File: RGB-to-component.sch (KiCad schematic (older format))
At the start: 56 parts, among them J1 VGA, J3 USB_C_Receptacle_Power, J4 SCART_CONN, J5 3xRCA_CONN, U1 SC6206B-65K5, U2 TPF144-VR, U3 RS8752XQ, U4 TPF-141TR, U6 74AHC1G86, U7 74AHC1G86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

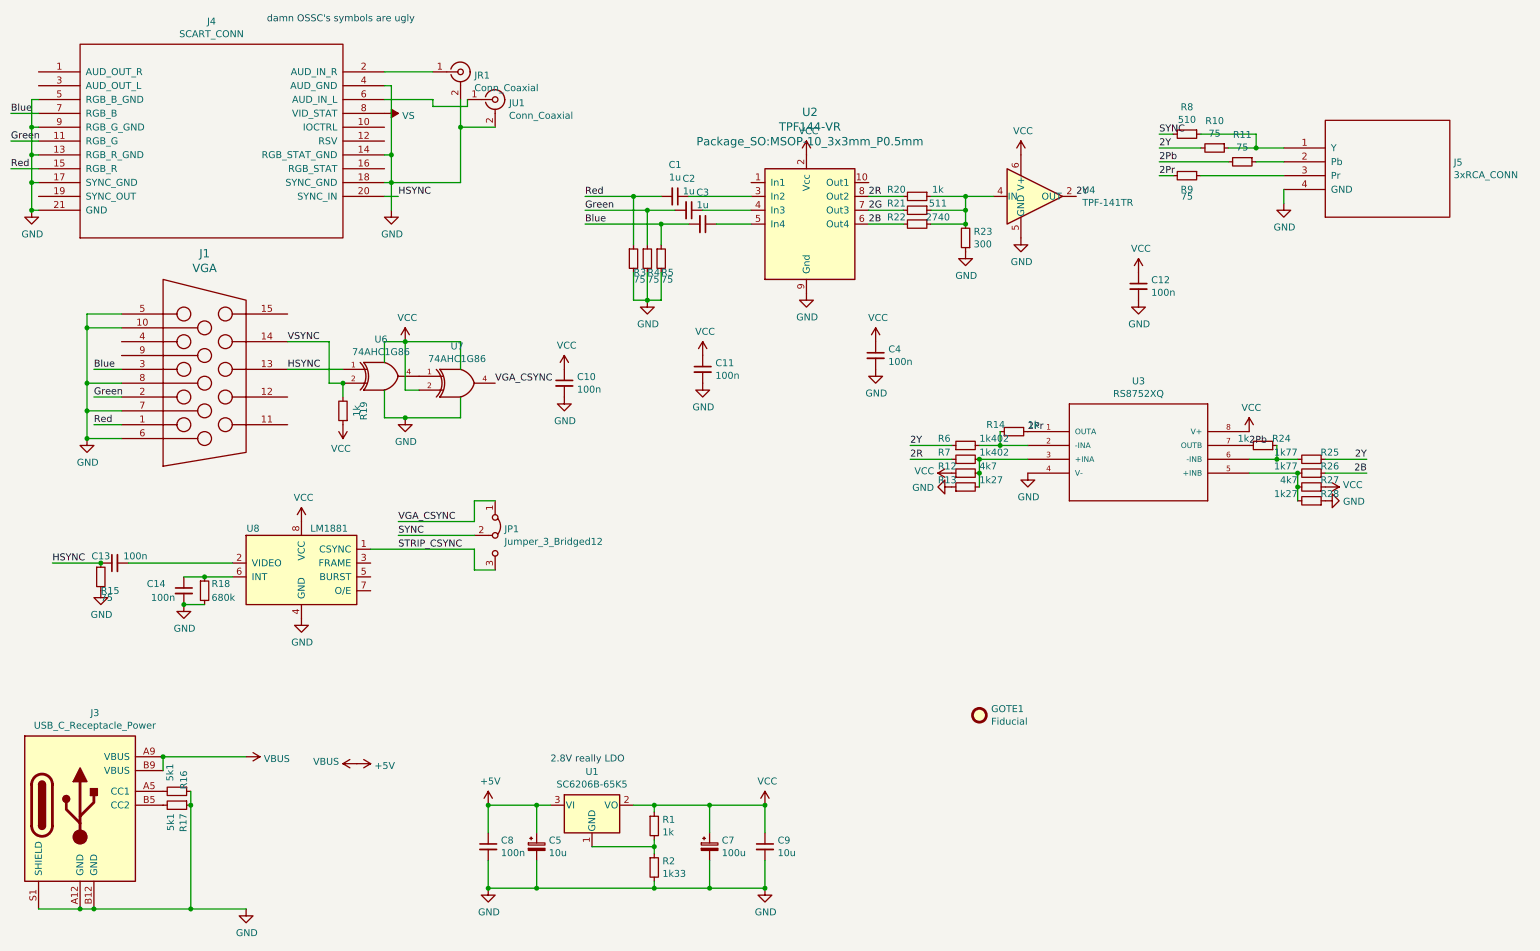
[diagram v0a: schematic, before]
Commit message: reusing video amp, ferrite, power led, updated jlc files
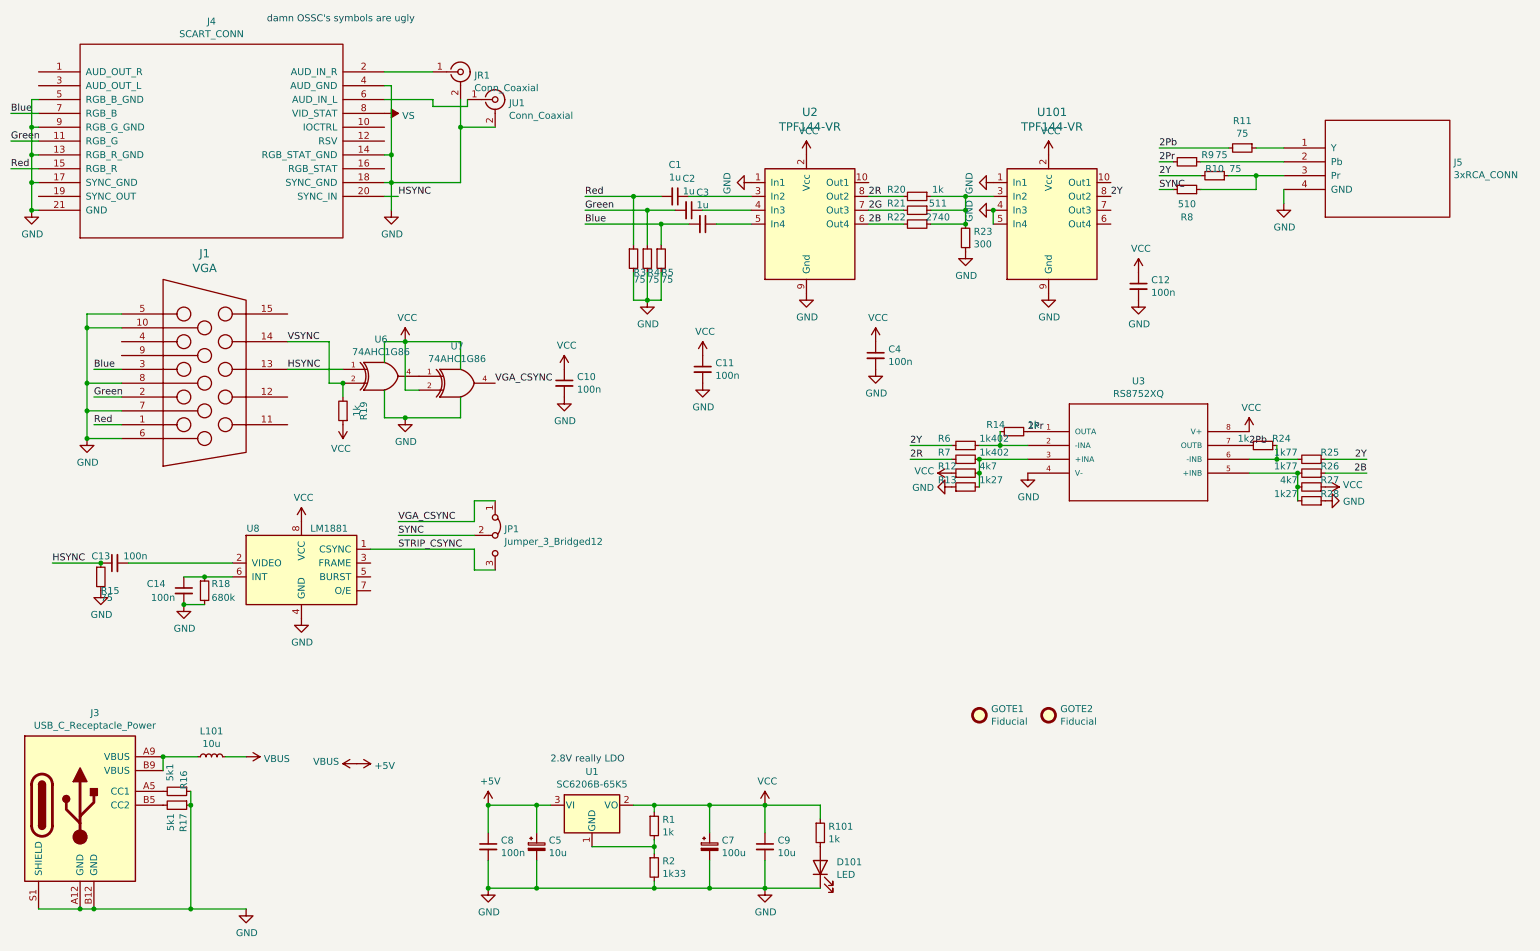
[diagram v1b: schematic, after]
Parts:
- removed U4: TPF-141TR, Package_TO_SOT_SMD:SOT-23-6, symbol Videobits:TPF-141TR
- added D101: LED, LED_SMD:LED_0805_2012Metric, symbol Device:LED
- added GOTE2: Fiducial, videobits:borgar, symbol Mechanical:Fiducial
- added L101: 10u, Inductor_SMD:L_0805_2012Metric_Pad1.15x1.40mm_HandSolder, symbol Device:L_Small
- added R101: 1k, Resistor_SMD:R_0805_2012Metric_Pad1.15x1.40mm_HandSolder, symbol Device:R_Small
- added U101: TPF144-VR, Package_SO:MSOP-10_3x3mm_P0.5mm, symbol Videobits:TPF144-VR
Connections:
- net +5V: now also L101.2; no longer J3.A9 (VBUS), J3.B9 (VBUS)
- net 2Y: now also U101.8 (Out2)
- net GND: now also U2.1 (In1), D101.1 (K), U101.1 (In1), U101.4 (In3), U101.5 (In4), U101.9 (Gnd)
- net VCC: now also R101.1, U101.2 (Vcc)
- net at R11.1: now also J5.1 (Y); no longer J5.2 (Pb)
- net at R10.1, R8.1: now also J5.3 (Pr); no longer J5.1 (Y)
- net at R9.1: now also J5.2 (Pb); no longer J5.3 (Pr)
- net at R20.1, R21.1, R22.1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: now also U101.3 (In2)
- new net: J3.A9 (VBUS), J3.B9 (VBUS), L101.1
- new net: D101.2 (A), R101.2
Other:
- moved on the sheet: R10, R11, R8, R9
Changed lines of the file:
@@
 L Device:R_Small R11
 U 1 1 5CA1152E
-P 9500 1650
-F 0 "R11" V 9304 1650 50  0000 C CNN
-F 1 "75" V 9395 1650 50  0000 C CNN
-F 2 "Resistor_SMD:R_0805_2012Metric_Pad1.15x1.40mm_HandSolder" H 9500 1650 50  0001 C CNN
-F 3 "~" H 9500 1650 50  0001 C CNN
-F 4 "C20638" H 9500 1650 50  0001 C CNN "LCSC"
-	1    9500 1650
+P 9500 1550
+F 0 "R11" V 9304 1550 50  0000 C CNN
+F 1 "75" V 9395 1550 50  0000 C CNN
+F 2 "Resistor_SMD:R_0805_2012Metric_Pad1.15x1.40mm_HandSolder" H 9500 1550 50  0001 C CNN
+F 3 "~" H 9500 1550 50  0001 C CNN
+F 4 "C20638" H 9500 1550 50  0001 C CNN "LCSC"
+	1    9500 1550
 	0    1    1    0
 $EndComp
@@
 L Device:R_Small R10
 U 1 1 5CA11A22
-P 9300 1550
-F 0 "R10" V 9104 1550 50  0000 C CNN
-F 1 "75" V 9195 1550 50  0000 C CNN
-F 2 "Resistor_SMD:R_0805_2012Metric_Pad1.15x1.40mm_HandSolder" H 9300 1550 50  0001 C CNN
-F 3 "~" H 9300 1550 50  0001 C CNN
-F 4 "C20638" H 9300 1550 50  0001 C CNN "LCSC"
-	1    9300 1550
-	0    1    1    0
+P 9300 1750
+F 0 "R10" V 9350 1750 50  0000 C CNN
+F 1 "75" V 9350 1900 50  0000 C CNN
+F 2 "Resistor_SMD:R_0805_2012Metric_Pad1.15x1.40mm_HandSolder" H 9300 1750 50  0001 C CNN
+F 3 "~" H 9300 1750 50  0001 C CNN
+F 4 "C20638" H 9300 1750 50  0001 C CNN "LCSC"
+	1    9300 1750
+	0    1    -1   0
 $EndComp
 $Comp
 L Device:R_Small R8
 U 1 1 5CA11F25
-P 9100 1450
-F 0 "R8" V 8904 1450 50  0000 C CNN
-F 1 "510" V 8995 1450 50  0000 C CNN
-F 2 "Resistor_SMD:R_0805_2012Metric_Pad1.15x1.40mm_HandSolder" H 9100 1450 50  0001 C CNN
-F 3 "~" H 9100 1450 50  0001 C CNN
-F 4 "C17734" H 9100 1450 50  0001 C CNN "LCSC"
-	1    9100 1450
-	0    1    1    0
+P 9100 1850
+F 0 "R8" V 8900 1850 50  0000 C CNN
+F 1 "510" V 8995 1850 50  0000 C CNN
+F 2 "Resistor_SMD:R_0805_2012Metric_Pad1.15x1.40mm_HandSolder" H 9100 1850 50  0001 C CNN
+F 3 "~" H 9100 1850 50  0001 C CNN
+F 4 "C17734" H 9100 1850 50  0001 C CNN "LCSC"
+	1    9100 1850
+	0    1    -1   0
 $EndComp
 $Comp
 L Device:R_Small R9
 U 1 1 5CA121BA
-P 9100 1750
-F 0 "R9" V 9200 1750 50  0000 C CNN
-F 1 "75" V 9250 1750 50  0000 C CNN
-F 2 "Resistor_SMD:R_0805_2012Metric_Pad1.15x1.40mm_HandSolder" H 9100 1750 50  0001 C CNN
-F 3 "~" H 9100 1750 50  0001 C CNN
-F 4 "C20638" H 9100 1750 50  0001 C CNN "LCSC"
-	1    9100 1750
+P 9100 1650
+F 0 "R9" V 9050 1800 50  0000 C CNN
+F 1 "75" V 9050 1900 50  0000 C CNN
+F 2 "Resistor_SMD:R_0805_2012Metric_Pad1.15x1.40mm_HandSolder" H 9100 1650 50  0001 C CNN
+F 3 "~" H 9100 1650 50  0001 C CNN
+F 4 "C20638" H 9100 1650 50  0001 C CNN "LCSC"
+	1    9100 1650
 	0    1    1    0
 $EndComp
 Wire Wire Line
-	8900 1550 9200 1550
-Wire Wire Line
-	9000 1450 8900 1450
-Wire Wire Line
-	9400 1650 8900 1650
-Wire Wire Line
-	9000 1750 8900 1750
+	8900 1750 9200 1750
+Wire Wire Line
+	9000 1850 8900 1850
+Wire Wire Line
+	9400 1550 8900 1550
+Wire Wire Line
+	9000 1650 8900 1650
 $Comp
 L power:GND #PWR06
@@
 	9800 1950 9800 1850
 Wire Wire Line
-	9800 1650 9600 1650
-Wire Wire Line
-	9400 1550 9600 1550
+	9800 1550 9600 1550
+Wire Wire Line
+	9400 1750 9600 1750
 $Comp
 L power:GND #PWR0109
@@
 	1700 6050 1700 5950
 Wire Wire Line
-	1700 5950 2300 5950
+	1700 5950 1950 5950
 Connection ~ 1700 5950
 $Comp
@@
 Connection ~ 1150 3650
 Wire Wire Line
-	9200 1450 9600 1450
-Wire Wire Line
-	9600 1450 9600 1550
-Connection ~ 9600 1550
-Wire Wire Line
-	9600 1550 9800 1550
+	9200 1850 9600 1850
+Wire Wire Line
+	9600 1850 9600 1750
+Connection ~ 9600 1750
+Wire Wire Line
+	9600 1750 9800 1750
 $Comp
 L Device:R_Small R18
@@
 $EndComp
 Wire Wire Line
-	9200 1750 9800 1750
-Text Label 8900 1550 0    50   ~ 0
+	9200 1650 9800 1650
+Text Label 8900 1750 0    50   ~ 0
 2Y
-Text Label 8900 1450 0    50   ~ 0
+Text Label 8900 1850 0    50   ~ 0
 SYNC
 $Comp
@@
 Text Label 9550 3700 0    50   ~ 0
 2Pb
+Text Label 8900 1550 0    50   ~ 0
+2Pb
 Text Label 8900 1650 0    50   ~ 0
-2Pb
-Text Label 8900 1750 0    50   ~ 0
 2Pr
 Connection ~ 5650 6300
@@
 L converted:VCC #PWR030
 U 1 1 5DAD195B
-P 7900 1600
-F 0 "#PWR030" H 7900 1450 50  0001 C CNN
-F 1 "VCC" H 7915 1773 50  0000 C CNN
-F 2 "" H 7900 1600 60  0000 C CNN
-F 3 "" H 7900 1600 60  0000 C CNN
-	1    7900 1600
+P 8100 1600
+F 0 "#PWR030" H 8100 1450 50  0001 C CNN
+F 1 "VCC" H 8115 1773 50  0000 C CNN
+F 2 "" H 8100 1600 60  0000 C CNN
+F 3 "" H 8100 1600 60  0000 C CNN
+	1    8100 1600
 	1    0    0    -1
 $EndComp
@@
 L power:GND #PWR031
 U 1 1 5DAD1F1E
-P 7900 2200
-F 0 "#PWR031" H 7900 1950 50  0001 C CNN
-F 1 "GND" H 7905 2027 50  0000 C CNN
-F 2 "" H 7900 2200 50  0001 C CNN
-F 3 "" H 7900 2200 50  0001 C CNN
-	1    7900 2200
-	1    0    0    -1
-$EndComp
-Text Label 8300 1900 0    50   ~ 0
+P 8100 2600
+F 0 "#PWR031" H 8100 2350 50  0001 C CNN
+F 1 "GND" H 8105 2427 50  0000 C CNN
+F 2 "" H 8100 2600 50  0001 C CNN
+F 3 "" H 8100 2600 50  0001 C CNN
+	1    8100 2600
+	1    0    0    -1
+$EndComp
+Text Label 8550 1900 0    50   ~ 0
 2Y
 Wire Wire Line
 	7700 1900 7500 1900
 Connection ~ 7500 1900
-$Comp
-L Videobits:TPF-141TR U4
-U 1 1 5DAEF7F6
-P 8000 1900
-F 0 "U4" H 8344 1946 50  0000 L CNN
-F 1 "TPF-141TR" H 8344 1855 50  0000 L CNN
-F 2 "Package_TO_SOT_SMD:SOT-23-6" H 8000 1900 50  0001 C CNN
-F 3 "" H 8000 1900 50  0001 C CNN
-F 4 "C155440" H 8000 1900 50  0001 C CNN "LCSC"
-	1    8000 1900
-	1    0    0    -1
-$EndComp
 $Comp
 L power:VCC #PWR0101
@@
 F 0 "U2" H 6375 3009 60  0000 C CNN
 F 1 "TPF144-VR" H 6375 2903 60  0000 C CNN
-F 2 "Package_SO:MSOP-10_3x3mm_P0.5mm" H 6375 2797 60  0000 C CNN
+F 2 "Package_SO:MSOP-10_3x3mm_P0.5mm" H 6375 2797 60  0001 C CNN
 F 3 "" H 6150 2400 60  0000 C CNN
 F 4 "C155447" H 6350 2150 50  0001 C CNN "LCSC"
@@
 Wire Wire Line
 	4400 6900 5250 6900
+$Comp
+L Videobits:TPF144-VR U101
+U 1 1 5ECB0808
+P 8100 2150
+F 0 "U101" H 8125 3009 60  0000 C CNN
+F 1 "TPF144-VR" H 8125 2903 60  0000 C CNN
+F 2 "Package_SO:MSOP-10_3x3mm_P0.5mm" H 8125 2797 60  0001 C CNN
+F 3 "" H 7900 2400 60  0000 C CNN
+F 4 "C155447" H 8100 2150 50  0001 C CNN "LCSC"
+	1    8100 2150
+	1    0    0    -1
+$EndComp
+$Comp
+L power:GND #PWR0102
+U 1 1 5ECC2FB3
+P 7700 2000
+F 0 "#PWR0102" H 7700 1750 50  0001 C CNN
+F 1 "GND" H 7705 1827 50  0000 C CNN
+F 2 "" H 7700 2000 50  0001 C CNN
+F 3 "" H 7700 2000 50  0001 C CNN
+	1    7700 2000
+	0    1    1    0
+$EndComp
+$Comp
+L power:GND #PWR0107
+U 1 1 5ECC4FBB
+P 7700 1800
+F 0 "#PWR0107" H 7700 1550 50  0001 C CNN
+F 1 "GND" H 7705 1627 50  0000 C CNN
+F 2 "" H 7700 1800 50  0001 C CNN
+F 3 "" H 7700 1800 50  0001 C CNN
+	1    7700 1800
+	0    1    1    0
+$EndComp
+$Comp
+L power:GND #PWR0111
+U 1 1 5ECC51CC
+P 5950 1800
+F 0 "#PWR0111" H 5950 1550 50  0001 C CNN
+F 1 "GND" H 5955 1627 50  0000 C CNN
+F 2 "" H 5950 1800 50  0001 C CNN
+F 3 "" H 5950 1800 50  0001 C CNN
+	1    5950 1800
+	0    1    1    0
+$EndComp
+Wire Wire Line
+	7700 2100 7700 2000
+Connection ~ 7700 2000
+$Comp
+L Device:LED D101
+U 1 1 5EEA1024
+P 6450 6750
+F 0 "D101" V 6489 6632 50  0000 R CNN
+F 1 "LED" V 6398 6632 50  0000 R CNN
+F 2 "LED_SMD:LED_0805_2012Metric" H 6450 6750 50  0001 C CNN
+F 3 "~" H 6450 6750 50  0001 C CNN
+F 4 "C34499" V 6450 6750 50  0001 C CNN "LCSC"
+	1    6450 6750
+	0    -1   -1   0
+$EndComp
+$Comp
+L Device:R_Small R101
+U 1 1 5EEA2303
+P 6450 6500
+F 0 "R101" H 6509 6546 50  0000 L CNN
+F 1 "1k" H 6509 6455 50  0000 L CNN
+F 2 "Resistor_SMD:R_0805_2012Metric_Pad1.15x1.40mm_HandSolder" H 6450 6500 50  0001 C CNN
+F 3 "~" H 6450 6500 50  0001 C CNN
+F 4 "C17513" H 6450 6500 50  0001 C CNN "LCSC"
+	1    6450 6500
+	1    0    0    -1
+$EndComp
+Wire Wire Line
+	6450 6900 6050 6900
+Wire Wire Line
+	6050 6300 6450 6300
+Wire Wire Line
+	6450 6300 6450 6400
+$Comp
+L Device:L_Small L101
+U 1 1 5EEB618A
+P 2050 5950
+F 0 "L101" V 2235 5950 50  0000 C CNN
+F 1 "10u" V 2144 5950 50  0000 C CNN
+F 2 "Inductor_SMD:L_0805_2012Metric_Pad1.15x1.40mm_HandSolder" H 2050 5950 50  0001 C CNN
+F 3 "~" H 2050 5950 50  0001 C CNN
+F 4 "C1046" V 2050 5950 50  0001 C CNN "LCSC"
+	1    2050 5950
+	0    -1   -1   0
+$EndComp
+Wire Wire Line
+	2150 5950 2300 5950
+$Comp
+L Mechanical:Fiducial GOTE2
+U 1 1 5EECD5AD
+P 8100 5650
+F 0 "GOTE2" H 8185 5696 50  0000 L CNN
+F 1 "Fiducial" H 8185 5605 50  0000 L CNN
+F 2 "videobits:borgar" H 8100 5650 50  0001 C CNN
+F 3 "~" H 8100 5650 50  0001 C CNN
+F 4 "NOT FITTED" H 8100 5650 50  0001 C CNN "LCSC"
+	1    8100 5650
+	1    0    0    -1
+$EndComp
 $EndSCHEMATC

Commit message: fixed resistor
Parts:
- R21: LCSC C55317 -> C273884
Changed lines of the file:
@@
 F 2 "Resistor_SMD:R_0805_2012Metric_Pad1.15x1.40mm_HandSolder" H 7150 2000 50  0001 C CNN
 F 3 "~" H 7150 2000 50  0001 C CNN
-F 4 "C55317" H 7150 2000 50  0001 C CNN "LCSC"
+F 4 "C273884" H 7150 2000 50  0001 C CNN "LCSC"
 	1    7150 2000
 	0    1    1    0

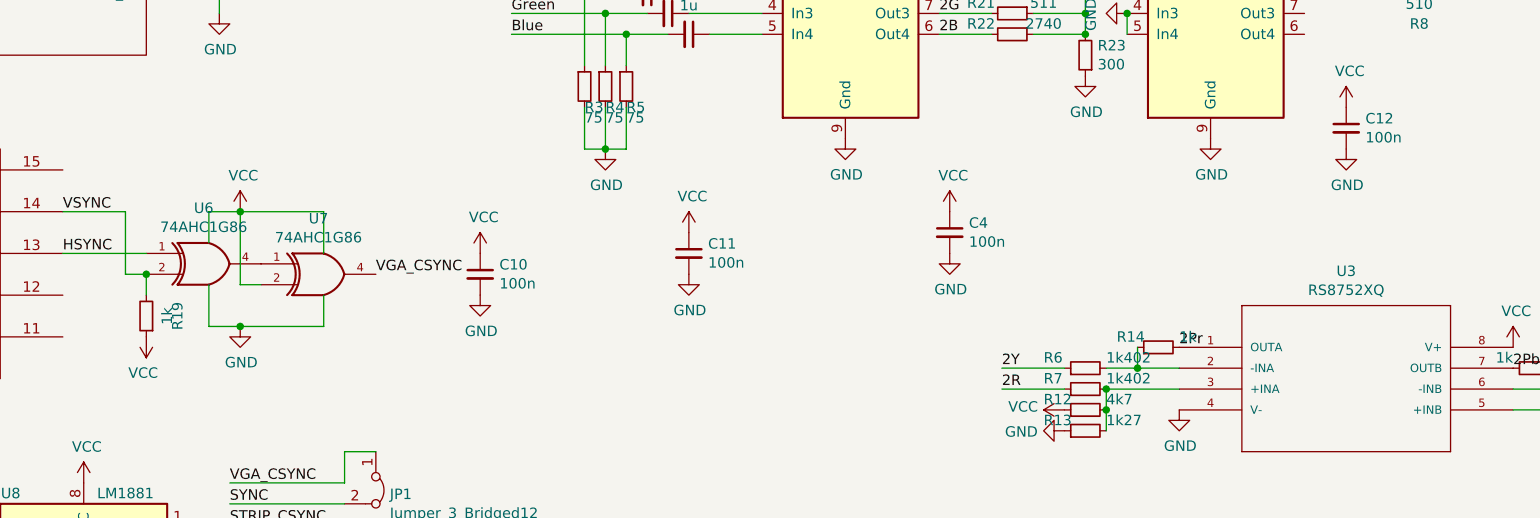
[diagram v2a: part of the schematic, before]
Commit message: changed RCA jacks to single centre pin style, AHCT gates for VGA sync
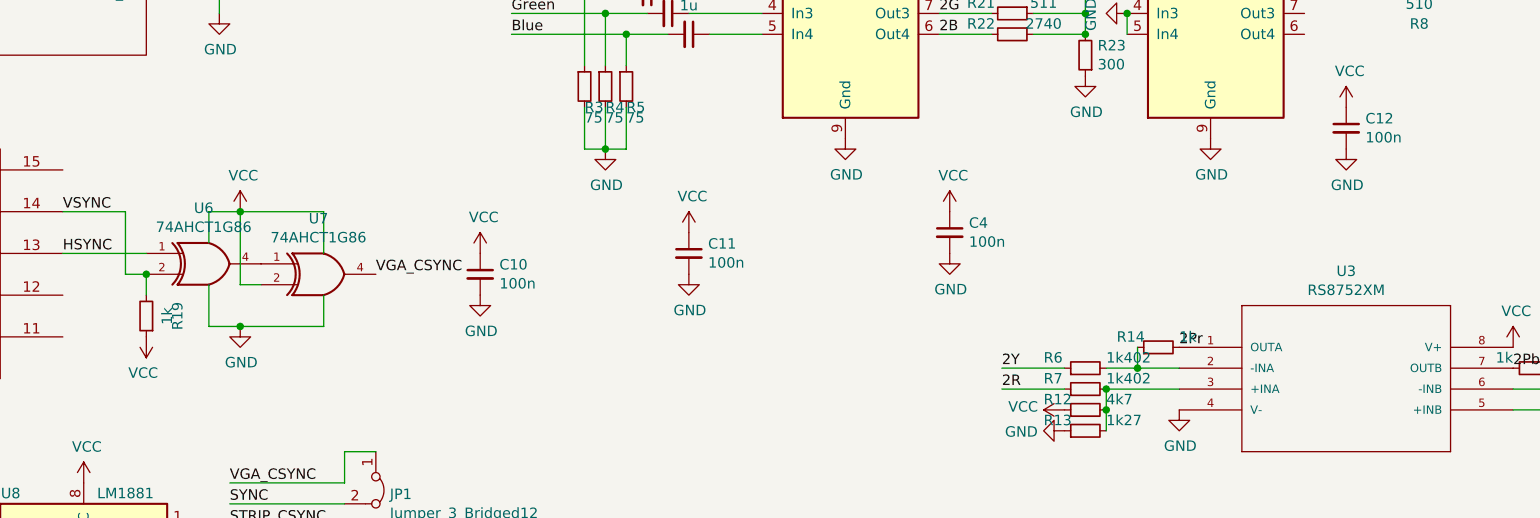
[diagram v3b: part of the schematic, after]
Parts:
- J5: footprint custom_components:3xRCA_CONN -> videobits:3xRCA_CONN_SINGLE
- U3: value RS8752XQ -> RS8752XM; footprint Package_SO:TSSOP-8_4.4x3mm_P0.65mm -> Package_SO:MSOP-8_3x3mm_P0.65mm; Field7 LT6206CMS8#PBF -> (none); Field8 MSOP-8 Linear Technology/Analog -> (none); LCSC C255422 -> C255421
- U6, U7: value 74AHC1G86 -> 74AHCT1G86; LCSC C7471 -> C43417
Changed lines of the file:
@@
 F 0 "J5" H 11028 1746 50  0000 L CNN
 F 1 "3xRCA_CONN" H 11028 1655 50  0000 L CNN
-F 2 "custom_components:3xRCA_CONN" H 10550 1700 50  0001 C CNN
+F 2 "videobits:3xRCA_CONN_SINGLE" H 10550 1700 50  0001 C CNN
 F 3 "" H 10550 1700 50  0001 C CNN
 F 4 "NOT FITTED" H 10550 1700 50  0001 C CNN "LCSC"
@@
 P 3300 3200
 F 0 "U6" H 3275 3467 50  0000 C CNN
-F 1 "74AHC1G86" H 3275 3376 50  0000 C CNN
+F 1 "74AHCT1G86" H 3275 3376 50  0000 C CNN
 F 2 "Package_TO_SOT_SMD:SOT-23-5" H 3300 3200 50  0001 C CNN
 F 3 "" H 3300 3200 50  0001 C CNN
-F 4 "C7471" H 3300 3200 50  0001 C CNN "LCSC"
+F 4 "C43417" H 3300 3200 50  0001 C CNN "LCSC"
 	1    3300 3200
 	1    0    0    -1
@@
 P 3850 3250
 F 0 "U7" H 3825 3517 50  0000 C CNN
-F 1 "74AHC1G86" H 3825 3426 50  0000 C CNN
+F 1 "74AHCT1G86" H 3825 3426 50  0000 C CNN
 F 2 "Package_TO_SOT_SMD:SOT-23-5" H 3850 3250 50  0001 C CNN
 F 3 "" H 3850 3250 50  0001 C CNN
-F 4 "C7471" H 3850 3250 50  0001 C CNN "LCSC"
+F 4 "C43417" H 3850 3250 50  0001 C CNN "LCSC"
 	1    3850 3250
 	1    0    0    -1
@@
 P 7950 3600
 F 0 "U3" H 8750 3965 50  0000 C CNN
-F 1 "RS8752XQ" H 8750 3874 50  0000 C CNN
-F 2 "Package_SO:TSSOP-8_4.4x3mm_P0.65mm" H 7950 3600 50  0001 L BNN
+F 1 "RS8752XM" H 8750 3874 50  0000 C CNN
+F 2 "Package_SO:MSOP-8_3x3mm_P0.65mm" H 7950 3600 50  0001 L BNN
 F 3 "" H 7950 3600 50  0001 L BNN
 F 4 "" H 7950 3600 50  0001 L BNN "Field4"
 F 5 "" H 7950 3600 50  0001 L BNN "Field5"
 F 6 "" H 7950 3600 50  0001 L BNN "Field6"
-F 7 "LT6206CMS8#PBF" H 7950 3600 50  0001 L BNN "Field7"
-F 8 "MSOP-8 Linear Technology/Analog" H 7950 3600 50  0001 L BNN "Field8"
-F 9 "C255422" H 7950 3600 50  0001 C CNN "LCSC"
+F 7 "" H 7950 3600 50  0001 L BNN "Field7"
+F 8 "" H 7950 3600 50  0000 L BNN "Field8"
+F 9 "C255421" H 7950 3600 50  0001 C CNN "LCSC"
 	1    7950 3600
 	1    0    0    -1
